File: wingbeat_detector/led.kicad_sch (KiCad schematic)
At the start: 7 parts, among them J2 CONN_UMC_JACK_SMD, Q1 MOSFET-N-CH, U6 LED_DRV_50mA

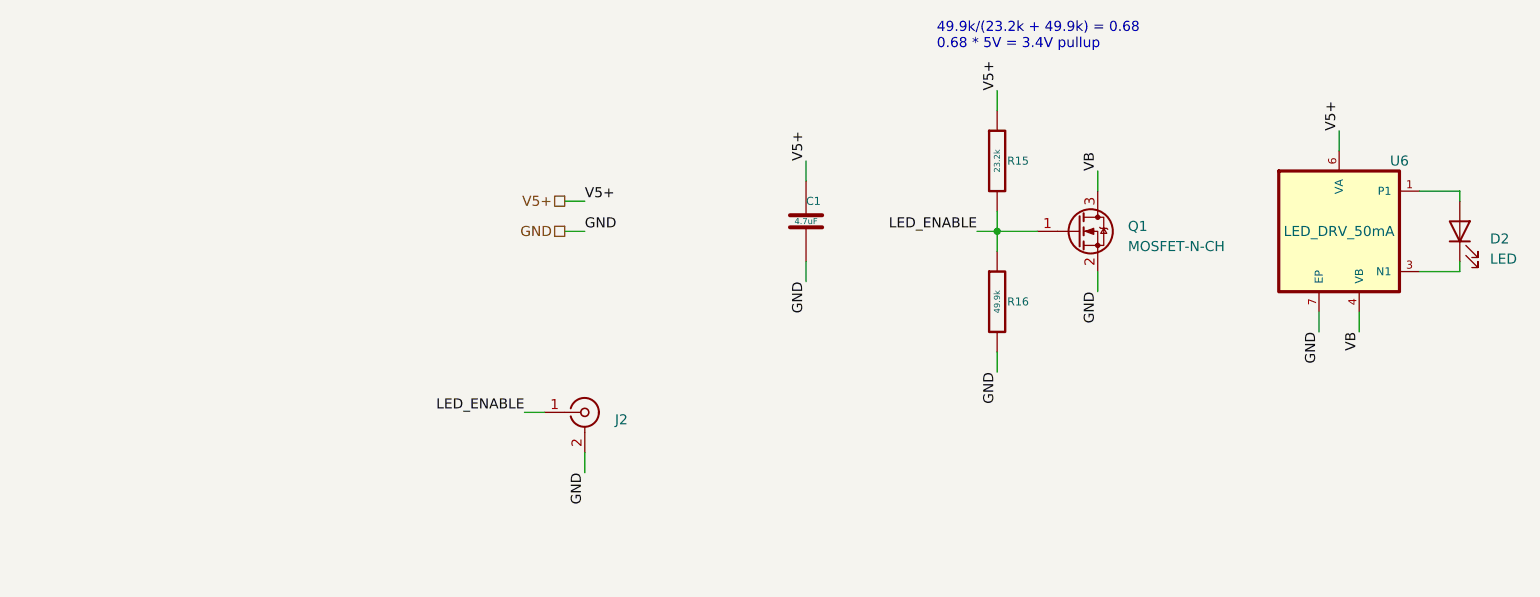
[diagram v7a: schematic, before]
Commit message: Finished routing tracks with no errors
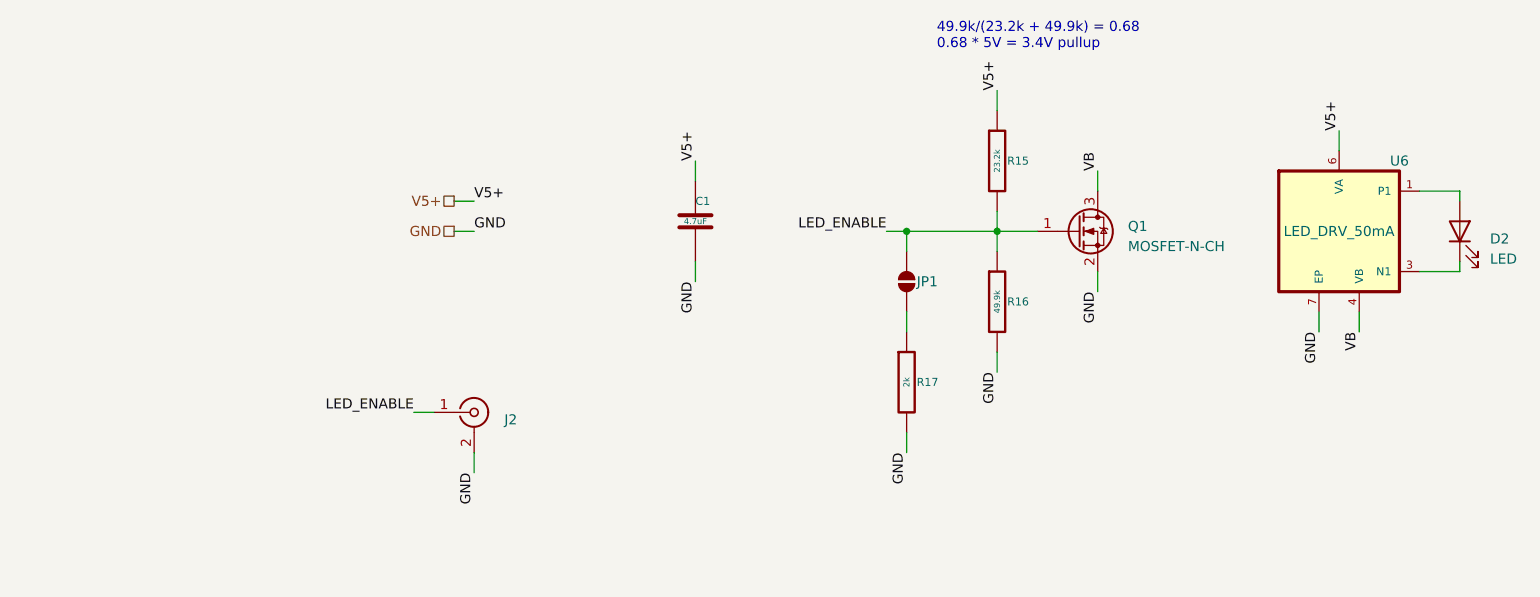
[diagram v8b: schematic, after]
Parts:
- added JP1: SolderJumper_2_Open, Janelia:SolderJumper-2_P1.3mm_Open_RoundedPad1.0x1.5mm, symbol Janelia:SolderJumper_2_Open
- added R17: 2k, Janelia:R_0402_1005Metric, symbol Janelia:R_2k_0402
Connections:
- net GND: now also R17.2
- net LED_ENABLE: now also JP1.2 (B)
- new net: JP1.1 (A), R17.1
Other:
- moved on the sheet: C1, J2
